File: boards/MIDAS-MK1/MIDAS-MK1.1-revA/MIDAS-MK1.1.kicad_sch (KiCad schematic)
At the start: 105 parts, among them J101 Left, J102 Right, J106 USB4105-GF-A, J107 DM3BT-DSF-PEJS, J108 Conn_01x02, J110 2157601003, J111 2157601003, SW101 SW_Push, SW102 SW_Push, U101 TCAL9539-Q1, U102 TCAL9539-Q1, U103 TCAL9539-Q1, U104 ESP32-S3-WROOM-1U, U105 MCP2518FDT-xSL, U106 MTFCxxxx, U107 TCAN337G, U108 ADS7138-Q1, U109 ECMF02-2AMX6, Y101 40MHz

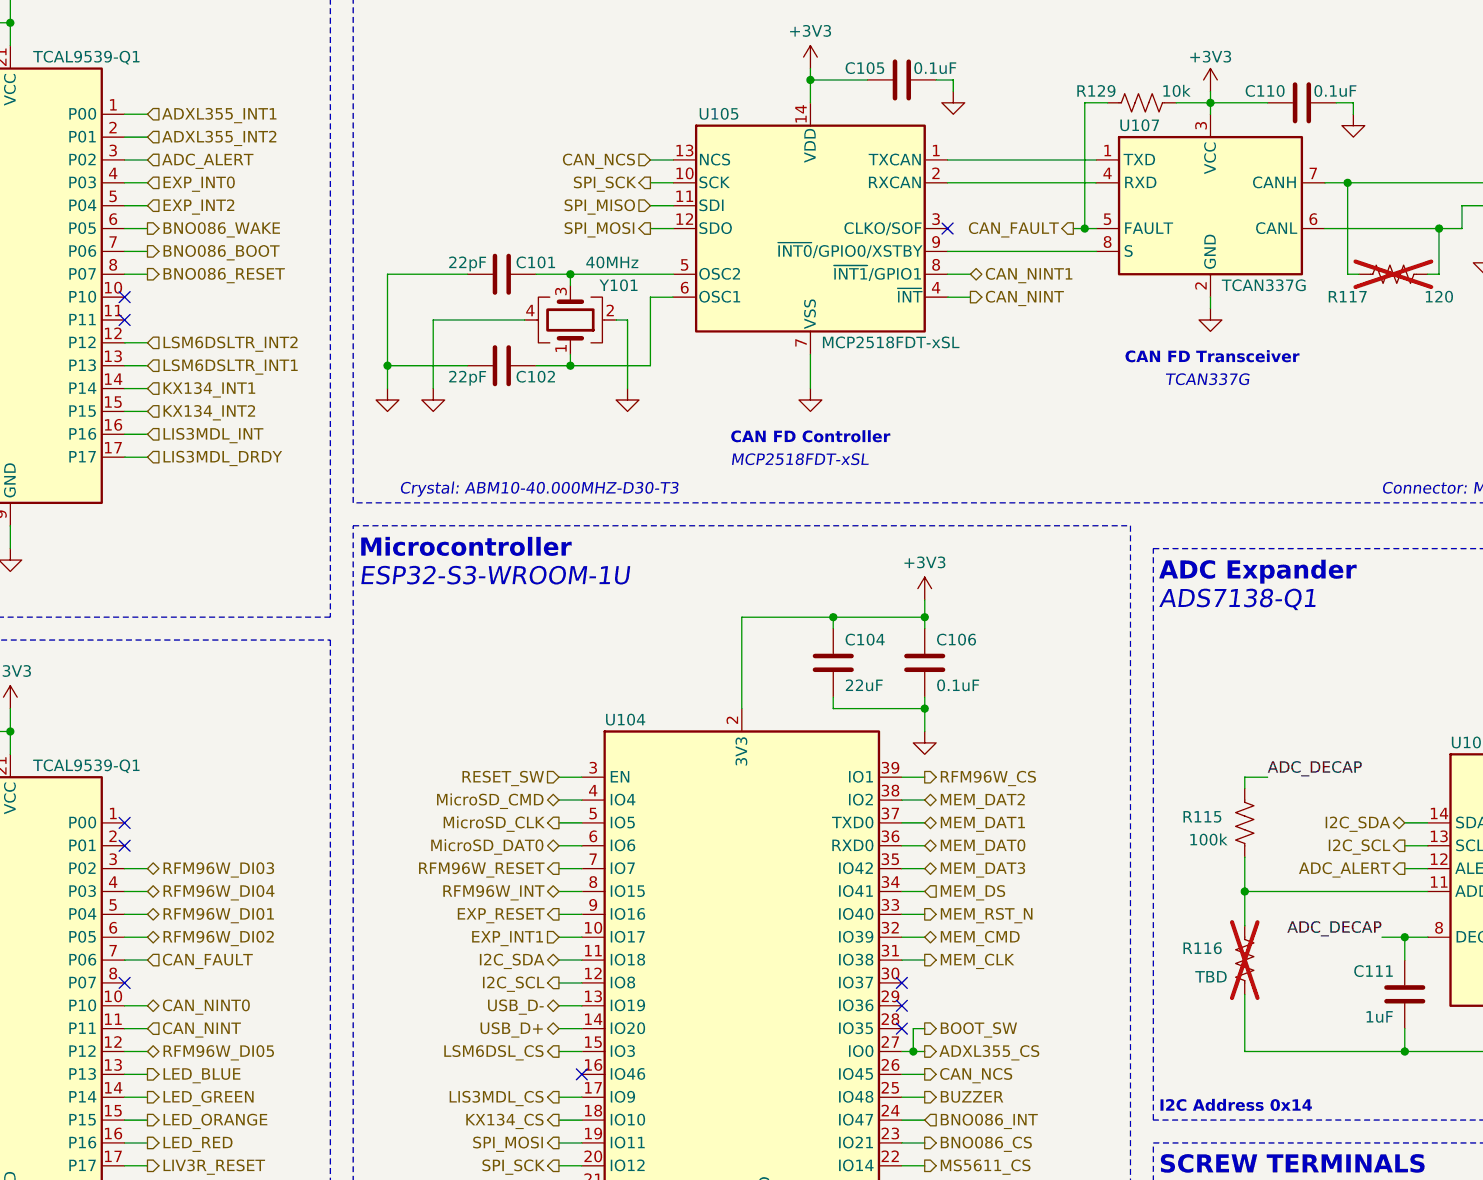
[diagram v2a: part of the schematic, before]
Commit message: finished major routing, made small schematic changes
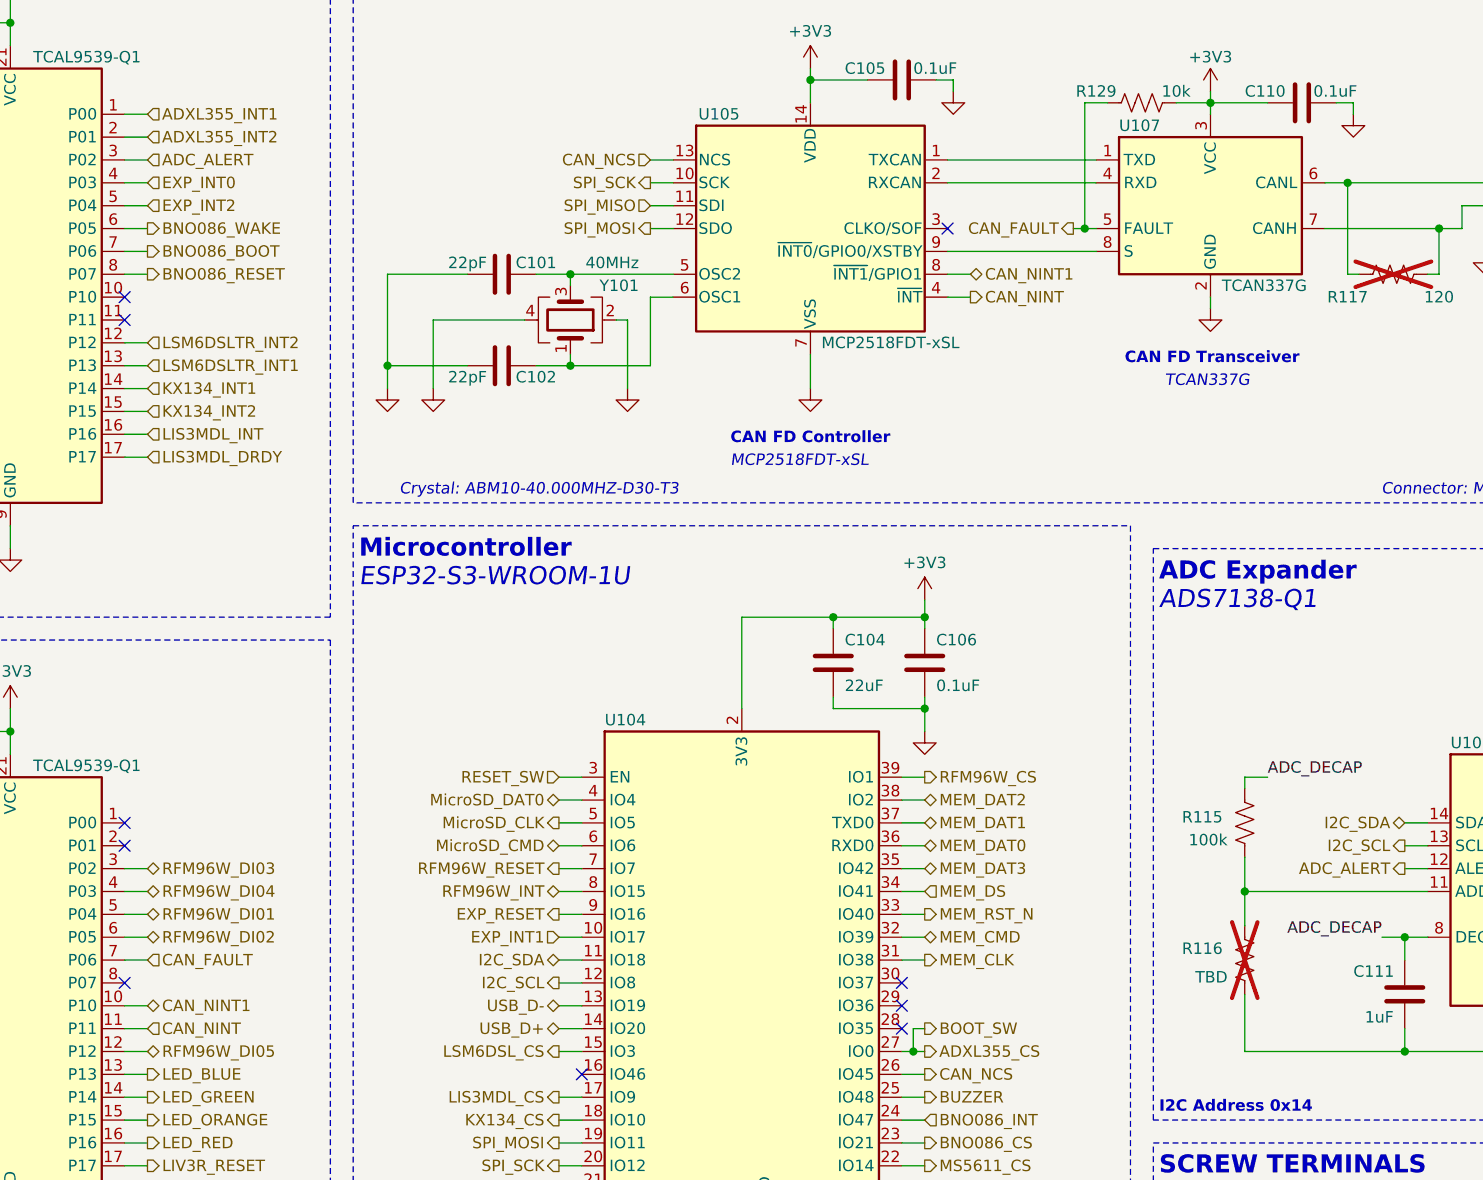
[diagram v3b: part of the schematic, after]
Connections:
- net CAN_NINT0 is gone; now on net CAN_NINT1: U103.10 (P10)
- net MicroSD_CMD: now also U104.6 (IO6); no longer U104.4 (IO4)
- net MicroSD_DAT0: now also U104.4 (IO4); no longer U104.6 (IO6)
- net at J110.1 (Pin_1), R117.2: now also U107.6 (CANL); no longer U107.7 (CANH)
- net at J110.2 (Pin_2), R117.1: now also U107.7 (CANH); no longer U107.6 (CANL)
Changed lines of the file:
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@@
     (effects (font (size 1.27 1.27)) (justify left))
+  )
+  (hierarchical_label "MicroSD_DAT0" (shape bidirectional) (at 109.22 190.5 180) (fields_autoplaced)
+    (effects (font (size 1.27 1.27)) (justify right))
   )
   (hierarchical_label "VBAT_PYRO" (shape output) (at 247.523 251.46 0) (fields_autoplaced)
@@
     (effects (font (size 1.27 1.27)) (justify left))
   )
-  (hierarchical_label "CAN_NINT0" (shape bidirectional) (at 63.5 213.36 0) (fields_autoplaced)
+  (hierarchical_label "CAN_NINT1" (shape bidirectional) (at 63.5 213.36 0) (fields_autoplaced)
     (effects (font (size 1.27 1.27)) (justify left))
   )
@@
     (effects (font (size 1.27 1.27)) (justify right))
   )
+  (hierarchical_label "MicroSD_CMD" (shape bidirectional) (at 109.22 195.58 180) (fields_autoplaced)
+    (effects (font (size 1.27 1.27)) (justify right))
+  )
   (hierarchical_label "ARM_A" (shape output) (at 63.5 71.12 0) (fields_autoplaced)
     (effects (font (size 1.27 1.27)) (justify left))
@@
     (effects (font (size 1.27 1.27)) (justify left))
   )
-  (hierarchical_label "MicroSD_CMD" (shape bidirectional) (at 109.22 190.5 180) (fields_autoplaced)
-    (effects (font (size 1.27 1.27)) (justify right))
-  )
   (hierarchical_label "EXP_RESET" (shape input) (at 55.88 279.4 0) (fields_autoplaced)
     (effects (font (size 1.27 1.27)) (justify left))
@@
     (effects (font (size 1.27 1.27)) (justify left))
   )
-  (hierarchical_label "MicroSD_DAT0" (shape bidirectional) (at 109.22 195.58 180) (fields_autoplaced)
-    (effects (font (size 1.27 1.27)) (justify right))
-  )
   (symbol (lib_id "Device:C") (at 370.84 77.47 0) (unit 1)

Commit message: changed terminal blocks and added U.FL/SMA footprint
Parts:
- J101, J102: footprint Connector_Molex_Terminal-Block:Molex_Terminal-Block_393570010_1x10_P3.5mm -> Connector_Phoenix_Terminal-Block:Phoenix_Terminal-Block_1751329_1x10_P3.5mm
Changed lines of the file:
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@@
       (effects (font (size 1.27 1.27)))
     )
-    (property "Footprint" "Connector_Molex_Terminal-Block:Molex_Terminal-Block_393570010_1x10_P3.5mm" (at 200.66 251.46 0)
-      (effects (font (size 1.27 1.27)) hide)
-    )
-    (property "Datasheet" "https://www.molex.com/en-us/products/part-detail/393570010?display=pdf" (at 200.66 251.46 0)
+    (property "Footprint" "Connector_Phoenix_Terminal-Block:Phoenix_Terminal-Block_1751329_1x10_P3.5mm" (at 200.66 251.46 0)
+      (effects (font (size 1.27 1.27)) hide)
+    )
+    (property "Datasheet" "https://www.phoenixcontact.com/en-us/products/printed-circuit-board-terminal-mkds-110-35-1751329" (at 200.66 251.46 0)
       (effects (font (size 1.27 1.27)) hide)
     )
@@
       (effects (font (size 1.27 1.27)))
     )
-    (property "Footprint" "Connector_Molex_Terminal-Block:Molex_Terminal-Block_393570010_1x10_P3.5mm" (at 237.363 254 0)
-      (effects (font (size 1.27 1.27)) hide)
-    )
-    (property "Datasheet" "https://www.molex.com/en-us/products/part-detail/393570010?display=pdf" (at 237.363 254 0)
-      (effects (font (size 1.27 1.27)) hide)
-    )
+    (property "Footprint" "Connector_Phoenix_Terminal-Block:Phoenix_Terminal-Block_1751329_1x10_P3.5mm" (at 237.363 254 0)
+      (effects (font (size 1.27 1.27)) hide)
+    )
+    (property "Datasheet" "https://www.phoenixcontact.com/en-us/products/printed-circuit-board-terminal-mkds-110-35-1751329" (at 237.363 254 0)
+      (effects (font (size 1.27 1.27)) hide)
+    )

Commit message: Minor Misc formatting/routing changes
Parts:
- H101, H102, H103, H104: symbol Mechanical:MountingHole -> Mechanical:MountingHole_Pad
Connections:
- no-connect marks 32 -> 36
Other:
- moved on the sheet: C101, C102
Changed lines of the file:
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@@
   (no_connect (at 129.54 58.42))
   (no_connect (at 162.56 53.34))
+  (no_connect (at 76.2 269.24))
   (no_connect (at 304.8 149.86))
   (no_connect (at 162.56 50.8))
@@
   (no_connect (at 129.54 50.8))
   (no_connect (at 129.54 53.34))
+  (no_connect (at 86.36 269.24))
+  (no_connect (at 76.2 276.86))
   (no_connect (at 60.96 134.62))
   (no_connect (at 292.1 154.94))
@@
   (no_connect (at 60.96 137.16))
   (no_connect (at 292.1 152.4))
+  (no_connect (at 86.36 276.86))
   (no_connect (at 162.56 58.42))
   (no_connect (at 162.56 45.72))
@@
     (stroke (width 0) (type default))
   )
-  (wire (pts (xy 110.49 132.08) (xy 106.68 132.08))
+  (wire (pts (xy 110.49 132.08) (xy 101.6 132.08))
     (stroke (width 0) (type default))
   )
@@
     (stroke (width 0) (type default))
   )
-  (wire (pts (xy 110.49 142.24) (xy 106.68 142.24))
+  (wire (pts (xy 110.49 142.24) (xy 101.6 142.24))
     (stroke (width 0) (type default))
   )
@@
     (stroke (width 0) (type default))
   )
-  (wire (pts (xy 99.06 142.24) (xy 90.17 142.24))
+  (wire (pts (xy 93.98 142.24) (xy 90.17 142.24))
     (stroke (width 0) (type default))
   )
@@
     (stroke (width 0) (type default))
   )
-  (wire (pts (xy 99.06 132.08) (xy 90.17 132.08))
+  (wire (pts (xy 93.98 132.08) (xy 90.17 132.08))
     (stroke (width 0) (type default))
   )
@@
     (stroke (width 0) (type default))
   )
-  (wire (pts (xy 105.41 137.16) (xy 95.25 137.16))
+  (wire (pts (xy 104.14 137.16) (xy 105.41 137.16))
     (stroke (width 0) (type default))
   )
@@
     (stroke (width 0) (type default))
   )
-  (wire (pts (xy 95.25 137.16) (xy 95.25 144.78))
+  (wire (pts (xy 104.14 137.16) (xy 104.14 144.78))
     (stroke (width 0) (type default))
   )
@@
     (fill (type none))
   )
-  (rectangle (start 71.12 264.16) (end 96.52 281.94)
+  (rectangle (start 71.12 256.54) (end 96.52 281.94)
     (stroke (width 0) (type dash))
     (fill (type none))
@@
     (effects (font (size 1.27 1.27)) (justify left bottom))
   )
-  (text "Mounting Holes" (at 71.755 267.97 0)
+  (text "Mounting Holes" (at 71.755 260.35 0)
     (effects (font (face "KiCad Font") (size 2 2) (thickness 0.4) bold) (justify left bottom))
   )
@@
     )
   )
-  (symbol (lib_id "Mechanical:MountingHole") (at 86.36 271.78 0) (unit 1)
+  (symbol (lib_id "Mechanical:MountingHole_Pad") (at 86.36 266.7 0) (unit 1)
     (in_bom yes) (on_board yes) (dnp no) (fields_autoplaced)
-    (property "Reference" "H103" (at 88.9 270.5679 0)
+    (property "Reference" "H103" (at 88.9 265.4879 0)
       (effects (font (size 1.27 1.27)) (justify left))
     )
-    (property "Value" "M3" (at 88.9 272.9921 0)
+    (property "Value" "M3" (at 88.9 267.9121 0)
       (effects (font (size 1.27 1.27)) (justify left))
     )
-    (property "Footprint" "MountingHole:MountingHole_3.2mm_M3_Pad_Via" (at 86.36 271.78 0)
+    (property "Footprint" "MountingHole:MountingHole_3.2mm_M3_Pad_Via" (at 86.36 266.7 0)
       (effects (font (size 1.27 1.27)) hide)
     )
-    (property "Datasheet" "~" (at 86.36 271.78 0)
+    (property "Datasheet" "~" (at 86.36 266.7 0)
       (effects (font (size 1.27 1.27)) hide)
     )
+    (pin "1")
     (instances
       (project "MIDAS-MK1.1"
@@
     )
   )
-  (symbol (lib_id "Device:C") (at 102.87 132.08 90) (mirror x) (unit 1)
+  (symbol (lib_id "Device:C") (at 97.79 132.08 90) (mirror x) (unit 1)
     (in_bom yes) (on_board yes) (dnp no)
-    (property "Reference" "C101" (at 106.68 130.81 90)
+    (property "Reference" "C101" (at 101.6 130.81 90)
       (effects (font (size 1.27 1.27)))
     )
-    (property "Value" "22pF" (at 99.06 130.81 90)
+    (property "Value" "22pF" (at 93.98 130.81 90)
       (effects (font (size 1.27 1.27)))
     )
-    (property "Footprint" "Capacitor_SMD:C_0603_1608Metric" (at 106.68 133.0452 0)
+    (property "Footprint" "Capacitor_SMD:C_0603_1608Metric" (at 101.6 133.0452 0)
       (effects (font (size 1.27 1.27)) hide)
     )
-    (property "Datasheet" "~" (at 102.87 132.08 0)
+    (property "Datasheet" "~" (at 97.79 132.08 0)
       (effects (font (size 1.27 1.27)) hide)
     )
@@
     )
   )
-  (symbol (lib_id "power:GND") (at 95.25 144.78 0) (mirror y) (unit 1)
+  (symbol (lib_id "power:GND") (at 104.14 144.78 0) (mirror y) (unit 1)
     (in_bom yes) (on_board yes) (dnp no) (fields_autoplaced)
-    (property "Reference" "#PWR0113" (at 95.25 151.13 0)
+    (property "Reference" "#PWR0113" (at 104.14 151.13 0)
       (effects (font (size 1.27 1.27)) hide)
     )
-    (property "Value" "GND" (at 95.25 148.9131 0)
+    (property "Value" "GND" (at 104.14 148.9131 0)
       (effects (font (size 1.27 1.27)) hide)
     )
-    (property "Footprint" "" (at 95.25 144.78 0)
+    (property "Footprint" "" (at 104.14 144.78 0)
       (effects (font (size 1.27 1.27)) hide)
     )
-    (property "Datasheet" "" (at 95.25 144.78 0)
+    (property "Datasheet" "" (at 104.14 144.78 0)
       (effects (font (size 1.27 1.27)) hide)
     )
@@
     )
   )
-  (symbol (lib_id "Device:C") (at 102.87 142.24 270) (mirror x) (unit 1)
+  (symbol (lib_id "Device:C") (at 97.79 142.24 270) (mirror x) (unit 1)
     (in_bom yes) (on_board yes) (dnp no)
-    (property "Reference" "C102" (at 106.68 143.51 90)
+    (property "Reference" "C102" (at 101.6 143.51 90)
       (effects (font (size 1.27 1.27)))
     )
-    (property "Value" "22pF" (at 99.06 143.51 90)
+    (property "Value" "22pF" (at 93.98 143.51 90)
       (effects (font (size 1.27 1.27)))
     )
-    (property "Footprint" "Capacitor_SMD:C_0603_1608Metric" (at 99.06 141.2748 0)
+    (property "Footprint" "Capacitor_SMD:C_0603_1608Metric" (at 93.98 141.2748 0)
       (effects (font (size 1.27 1.27)) hide)
     )
-    (property "Datasheet" "~" (at 102.87 142.24 0)
+    (property "Datasheet" "~" (at 97.79 142.24 0)
       (effects (font (size 1.27 1.27)) hide)
     )
@@
     )
   )
-  (symbol (lib_id "Mechanical:MountingHole") (at 86.36 276.86 0) (unit 1)
+  (symbol (lib_id "Mechanical:MountingHole_Pad") (at 86.36 274.32 0) (unit 1)
     (in_bom yes) (on_board yes) (dnp no) (fields_autoplaced)
-    (property "Reference" "H104" (at 88.9 275.6479 0)
+    (property "Reference" "H104" (at 88.9 273.1079 0)
       (effects (font (size 1.27 1.27)) (justify left))
     )
-    (property "Value" "M3" (at 88.9 278.0721 0)
+    (property "Value" "M3" (at 88.9 275.5321 0)
       (effects (font (size 1.27 1.27)) (justify left))
     )
-    (property "Footprint" "MountingHole:MountingHole_3.2mm_M3_Pad_Via" (at 86.36 276.86 0)
+    (property "Footprint" "MountingHole:MountingHole_3.2mm_M3_Pad_Via" (at 86.36 274.32 0)
       (effects (font (size 1.27 1.27)) hide)
     )
-    (property "Datasheet" "~" (at 86.36 276.86 0)
+    (property "Datasheet" "~" (at 86.36 274.32 0)
       (effects (font (size 1.27 1.27)) hide)
     )
+    (pin "1")
     (instances
       (project "MIDAS-MK1.1"
@@
     )
   )
-  (symbol (lib_id "Mechanical:MountingHole") (at 76.2 271.78 0) (unit 1)
+  (symbol (lib_id "Mechanical:MountingHole_Pad") (at 76.2 266.7 0) (unit 1)
     (in_bom yes) (on_board yes) (dnp no) (fields_autoplaced)
-    (property "Reference" "H101" (at 78.74 270.5679 0)
+    (property "Reference" "H101" (at 78.74 265.4879 0)
       (effects (font (size 1.27 1.27)) (justify left))
     )
-    (property "Value" "M3" (at 78.74 272.9921 0)
+    (property "Value" "M3" (at 78.74 267.9121 0)
       (effects (font (size 1.27 1.27)) (justify left))
     )
-    (property "Footprint" "MountingHole:MountingHole_3.2mm_M3_Pad_Via" (at 76.2 271.78 0)
+    (property "Footprint" "MountingHole:MountingHole_3.2mm_M3_Pad_Via" (at 76.2 266.7 0)
       (effects (font (size 1.27 1.27)) hide)
     )
-    (property "Datasheet" "~" (at 76.2 271.78 0)
+    (property "Datasheet" "~" (at 76.2 266.7 0)
       (effects (font (size 1.27 1.27)) hide)
     )
+    (pin "1")
     (instances
       (project "MIDAS-MK1.1"
@@
   (symbol (lib_id "Device:Crystal_GND24") (at 110.49 137.16 270) (mirror x) (unit 1)
     (in_bom yes) (on_board yes) (dnp no)
-    (property "Reference" "Y101" (at 118.11 133.35 90)
-      (effects (font (size 1.27 1.27)) (justify right))
+    (property "Reference" "Y101" (at 114.3 133.35 90)
+      (effects (font (size 1.27 1.27)))
     )
-    (property "Value" "40MHz" (at 118.11 130.81 90)
-      (effects (font (size 1.27 1.27)) (justify right))
+    (property "Value" "40MHz" (at 114.3 130.81 90)
+      (effects (font (size 1.27 1.27)))
     )
     (property "Footprint" "Crystal:Crystal_SMD_Abracon_ABM10-4Pin_2.5x2.0mm" (at 110.49 137.16 0)
@@
     )
   )
-  (symbol (lib_id "Mechanical:MountingHole") (at 76.2 276.86 0) (unit 1)
+  (symbol (lib_id "Mechanical:MountingHole_Pad") (at 76.2 274.32 0) (unit 1)
     (in_bom yes) (on_board yes) (dnp no) (fields_autoplaced)
-    (property "Reference" "H102" (at 78.74 275.6479 0)
+    (property "Reference" "H102" (at 78.74 273.1079 0)
       (effects (font (size 1.27 1.27)) (justify left))
     )
-    (property "Value" "M3" (at 78.74 278.0721 0)
+    (property "Value" "M3" (at 78.74 275.5321 0)
       (effects (font (size 1.27 1.27)) (justify left))
     )
-    (property "Footprint" "MountingHole:MountingHole_3.2mm_M3_Pad_Via" (at 76.2 276.86 0)
+    (property "Footprint" "MountingHole:MountingHole_3.2mm_M3_Pad_Via" (at 76.2 274.32 0)
       (effects (font (size 1.27 1.27)) hide)
     )
-    (property "Datasheet" "~" (at 76.2 276.86 0)
+    (property "Datasheet" "~" (at 76.2 274.32 0)
       (effects (font (size 1.27 1.27)) hide)
     )
+    (pin "1")
     (instances
       (project "MIDAS-MK1.1"
